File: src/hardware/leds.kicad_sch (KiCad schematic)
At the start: 74 parts

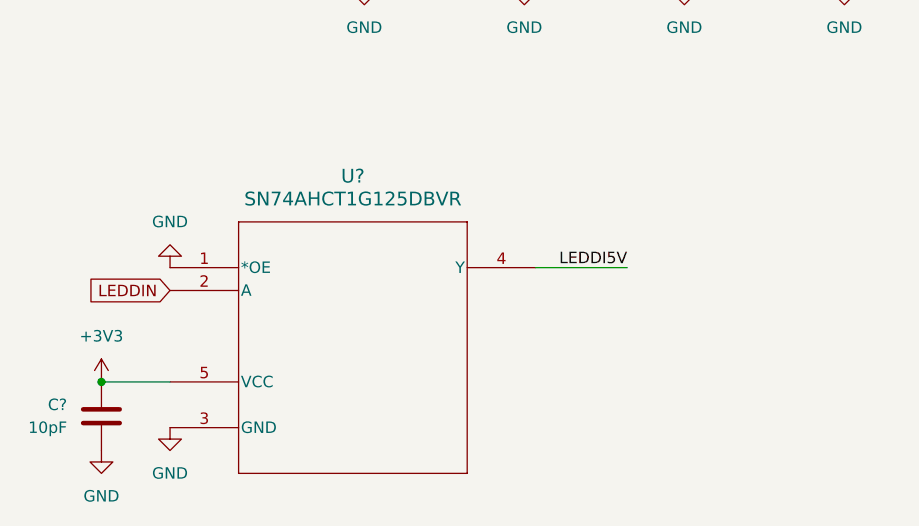
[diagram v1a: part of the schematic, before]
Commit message: Replaced schematics, 3d models and footprints. Added vibration motor.
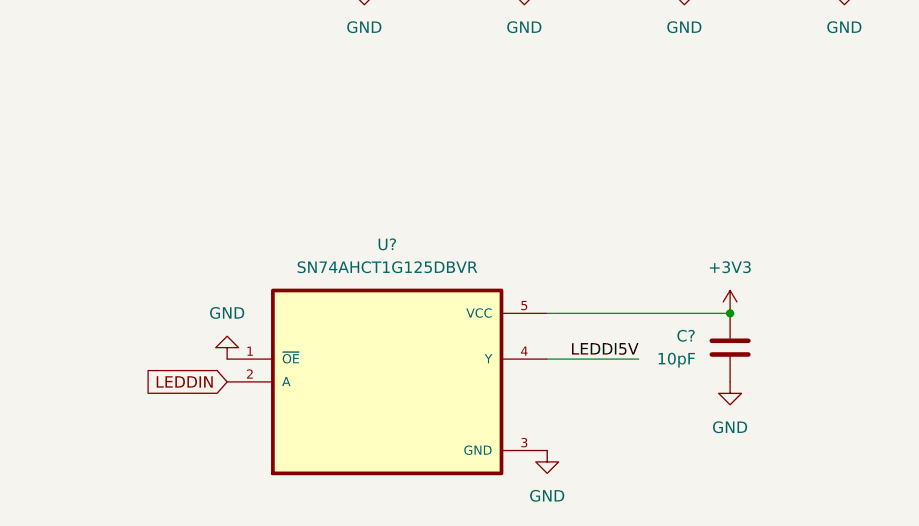
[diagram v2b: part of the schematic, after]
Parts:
- removed U?: SN74AHCT1G125DBVR, DBV5, symbol SN74AHCT1G125DBVR:SN74AHCT1G125DBVR
- added U?: SN74AHCT1G125DBVR, SN74AHCT1G125DBVR:SOT95P280X145-5N, symbol SN74AHCT1G125DBVR:SN74AHCT1G125DBVR
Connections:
- net +3V3: now also U?.5 (VCC)
- net GND: now also U?.1 (~{OE}), U?.3 (GND)
- net LEDDI5V: now also U?.4 (Y)
- net LEDDIN: now also U?.2 (A)
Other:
- moved on the sheet: C?

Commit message: Added LoRa
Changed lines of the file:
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@@
 		)
 		(property "Value" "+5V"
-			(at 48.26 31.75 0)
-			(effects
-				(font
-					(size 1.27 1.27)
-				)
+			(at 45.72 35.5599 0)
+			(effects
+				(font
+					(size 1.27 1.27)
+				)
+				(justify right)
 			)
 		)
@@
 		(fields_autoplaced yes)
 		(property "Reference" "C?"
-			(at 97.79 167.6399 0)
-			(effects
-				(font
-					(size 1.27 1.27)
-				)
-				(justify left)
+			(at 105.41 167.6399 0)
+			(effects
+				(font
+					(size 1.27 1.27)
+				)
+				(justify right)
 			)
 		)
 		(property "Value" "10pF"
-			(at 97.79 170.1799 0)
-			(effects
-				(font
-					(size 1.27 1.27)
-				)
-				(justify left)
+			(at 105.41 170.1799 0)
+			(effects
+				(font
+					(size 1.27 1.27)
+				)
+				(justify right)
 			)
 		)
@@
 		)
 		(property "Value" "GND"
-			(at 45.72 165.1 0)
-			(effects
-				(font
-					(size 1.27 1.27)
-				)
-			)
-		)
+			(at 43.18 168.9099 0)
+			(effects
+				(font
+					(size 1.27 1.27)
+				)
+				(justify right)
+			)
+		)

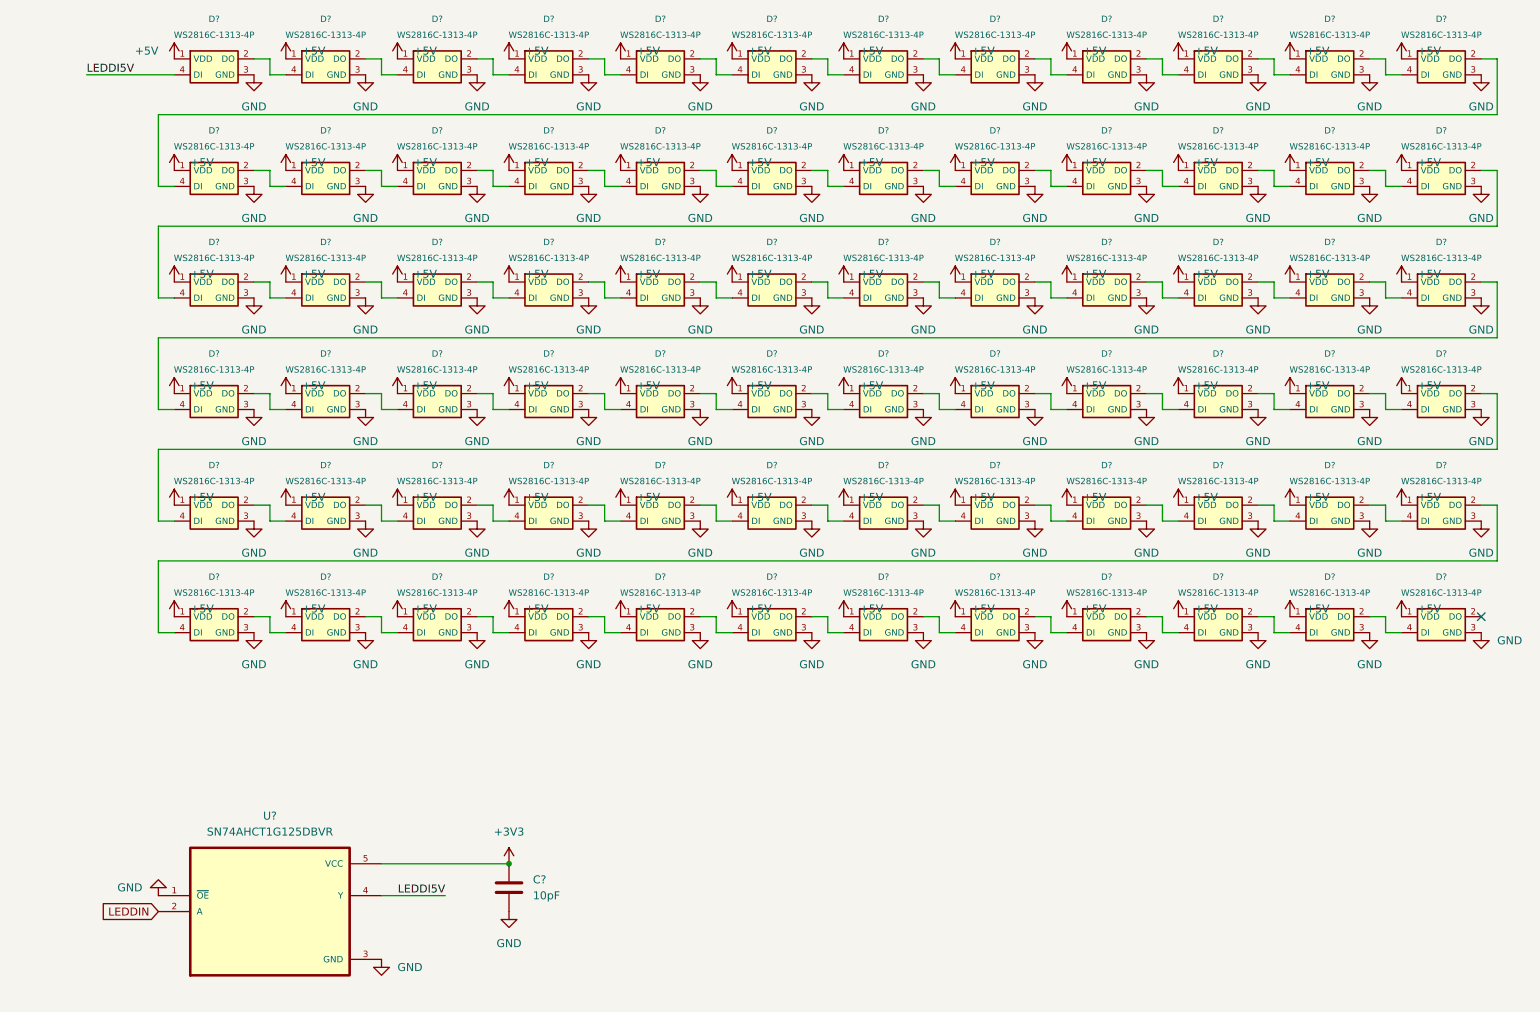
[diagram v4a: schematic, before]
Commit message: Changed 5V net to 4.5V net
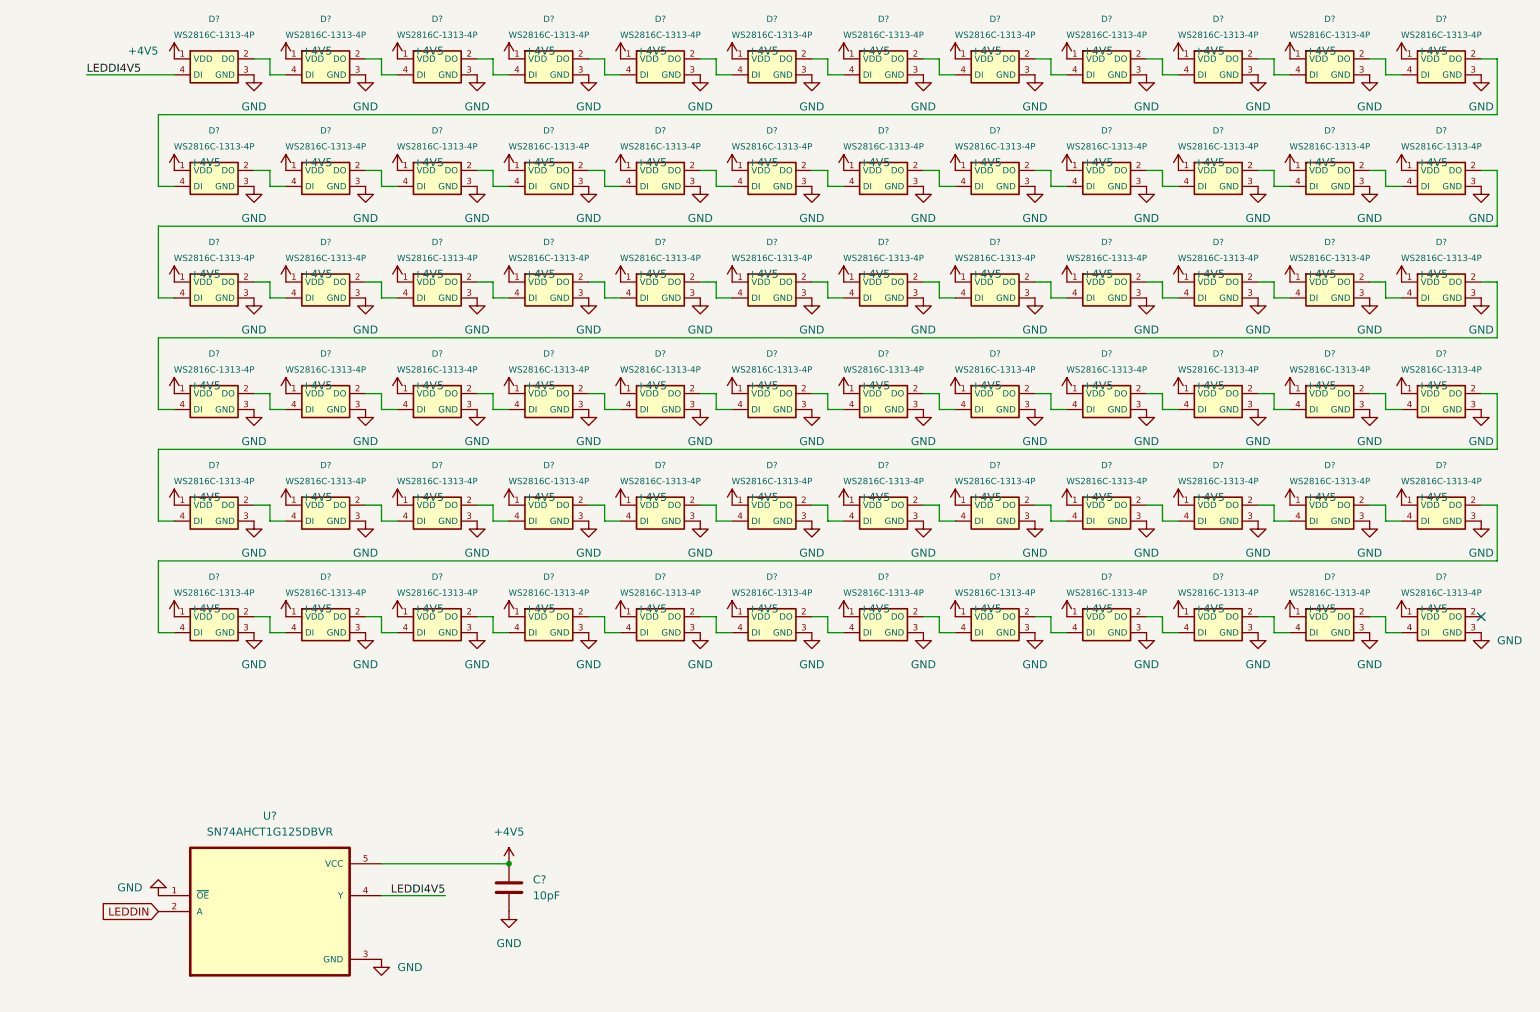
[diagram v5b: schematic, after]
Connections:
- net +5V is gone; now on net +4V5: D?.1 (VDD), D?.1 (VDD), D?.1 (VDD), D?.1 (VDD), D?.1 (VDD), D?.1 (VDD), D?.1 (VDD), D?.1 (VDD), D?.1 (VDD), D?.1 (VDD), D?.1 (VDD), D?.1 (VDD), D?.1 (VDD), D?.1 (VDD), D?.1 (VDD), D?.1 (VDD), D?.1 (VDD), D?.1 (VDD), D?.1 (VDD), D?.1 (VDD), D?.1 (VDD), D?.1 (VDD), D?.1 (VDD), D?.1 (VDD), D?.1 (VDD), D?.1 (VDD), D?.1 (VDD), D?.1 (VDD), D?.1 (VDD), D?.1 (VDD), D?.1 (VDD), D?.1 (VDD), D?.1 (VDD), D?.1 (VDD), D?.1 (VDD), D?.1 (VDD), D?.1 (VDD), D?.1 (VDD), D?.1 (VDD), D?.1 (VDD), D?.1 (VDD), D?.1 (VDD), D?.1 (VDD), D?.1 (VDD), D?.1 (VDD), D?.1 (VDD), D?.1 (VDD), D?.1 (VDD), D?.1 (VDD), D?.1 (VDD), D?.1 (VDD), D?.1 (VDD), D?.1 (VDD), D?.1 (VDD), D?.1 (VDD), D?.1 (VDD), D?.1 (VDD), D?.1 (VDD), D?.1 (VDD), D?.1 (VDD), D?.1 (VDD), D?.1 (VDD), D?.1 (VDD), D?.1 (VDD), D?.1 (VDD), D?.1 (VDD), D?.1 (VDD), D?.1 (VDD), D?.1 (VDD), D?.1 (VDD), D?.1 (VDD), D?.1 (VDD)
- net +3V3 renamed +4V5
- net LEDDI5V renamed LEDDI4V5

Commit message: Cleanup & Fixes; Added footprints; Removed Light sensors
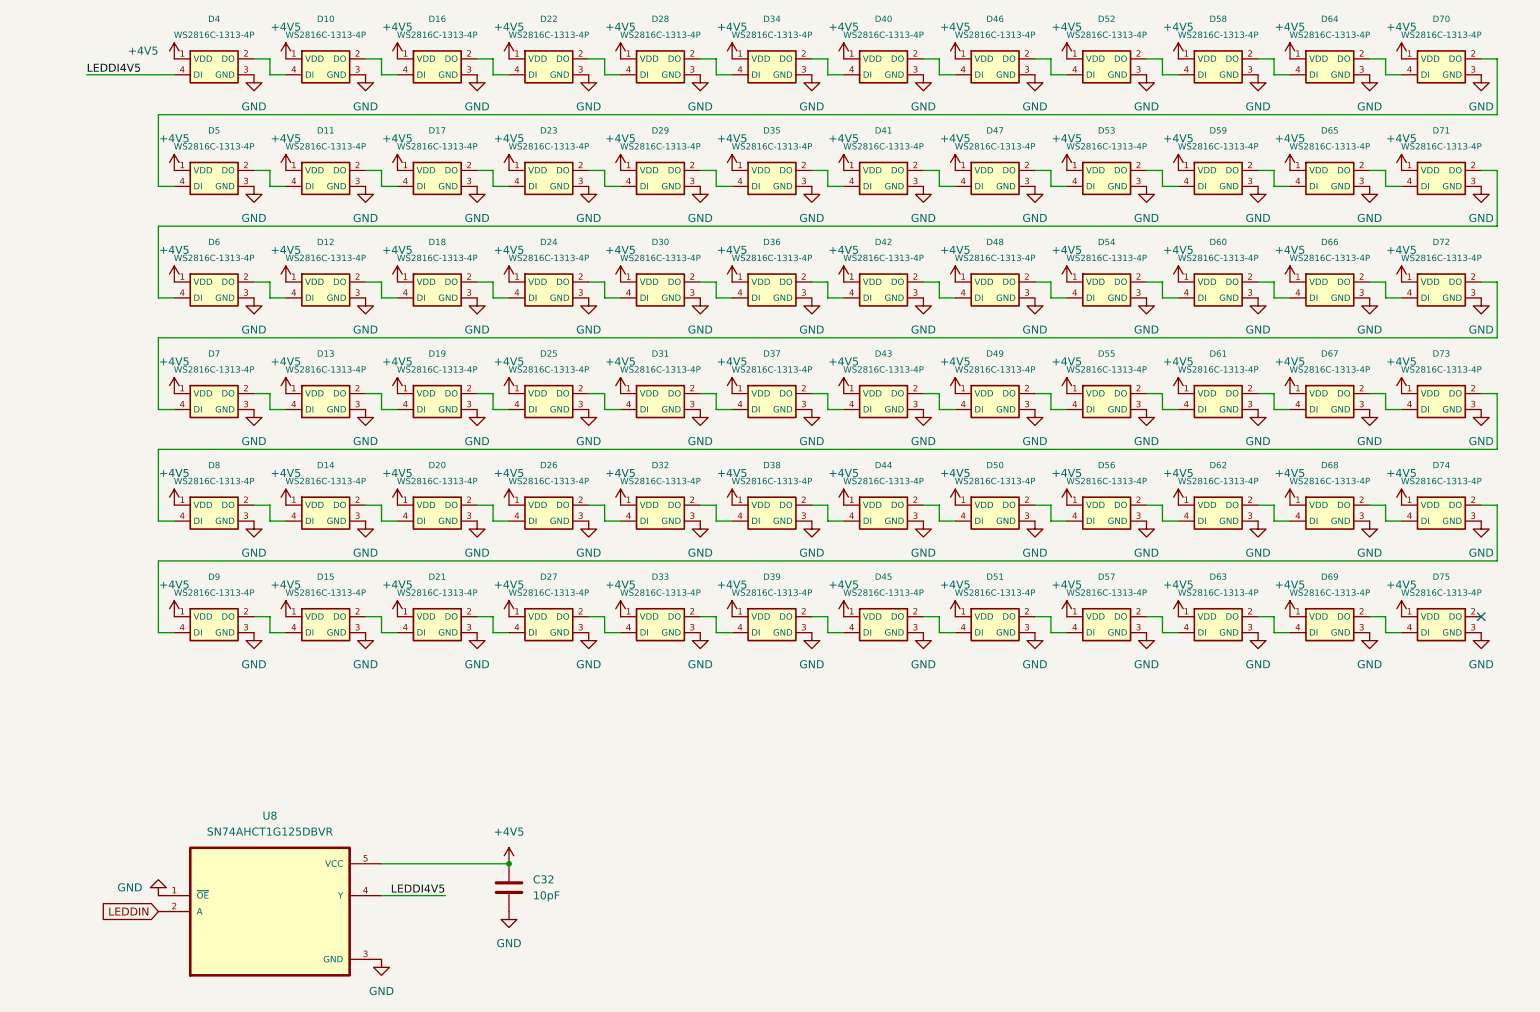
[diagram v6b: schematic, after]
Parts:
- C32: renamed from C?; footprint (none) -> Capacitor_SMD:C_0603_1608Metric
- D10, D11, D12, D13, D14, D15, D16, D17, D18, D19, D20, D21, D22, D23, D24, D25, D26, D27, D28, D29, D30, D31, D32, D33, D34, D35, D36, D37, D38, D39, D4, D40, D41, D42, D43, D44, D45, D46, D47, D48, D49, D5, D50, D51, D52, D53, D54, D55, D56, D57, D58, D59, D6, D60, D61, D62, D63, D64, D65, D66, D67, D68, D69, D7, D70, D71, D72, D73, D74, D75, D8, D9: renamed from D?; footprint WS2816C:WS2816C-1313-4P -> Project:WS2816C-1313-4P
- U8: renamed from U?; footprint SN74AHCT1G125DBVR:SOT95P280X145-5N -> Project:SOT95P280X145-5N

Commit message: Cleanup & Fixes; Changed GPIO; Added Camera; Added Microphone
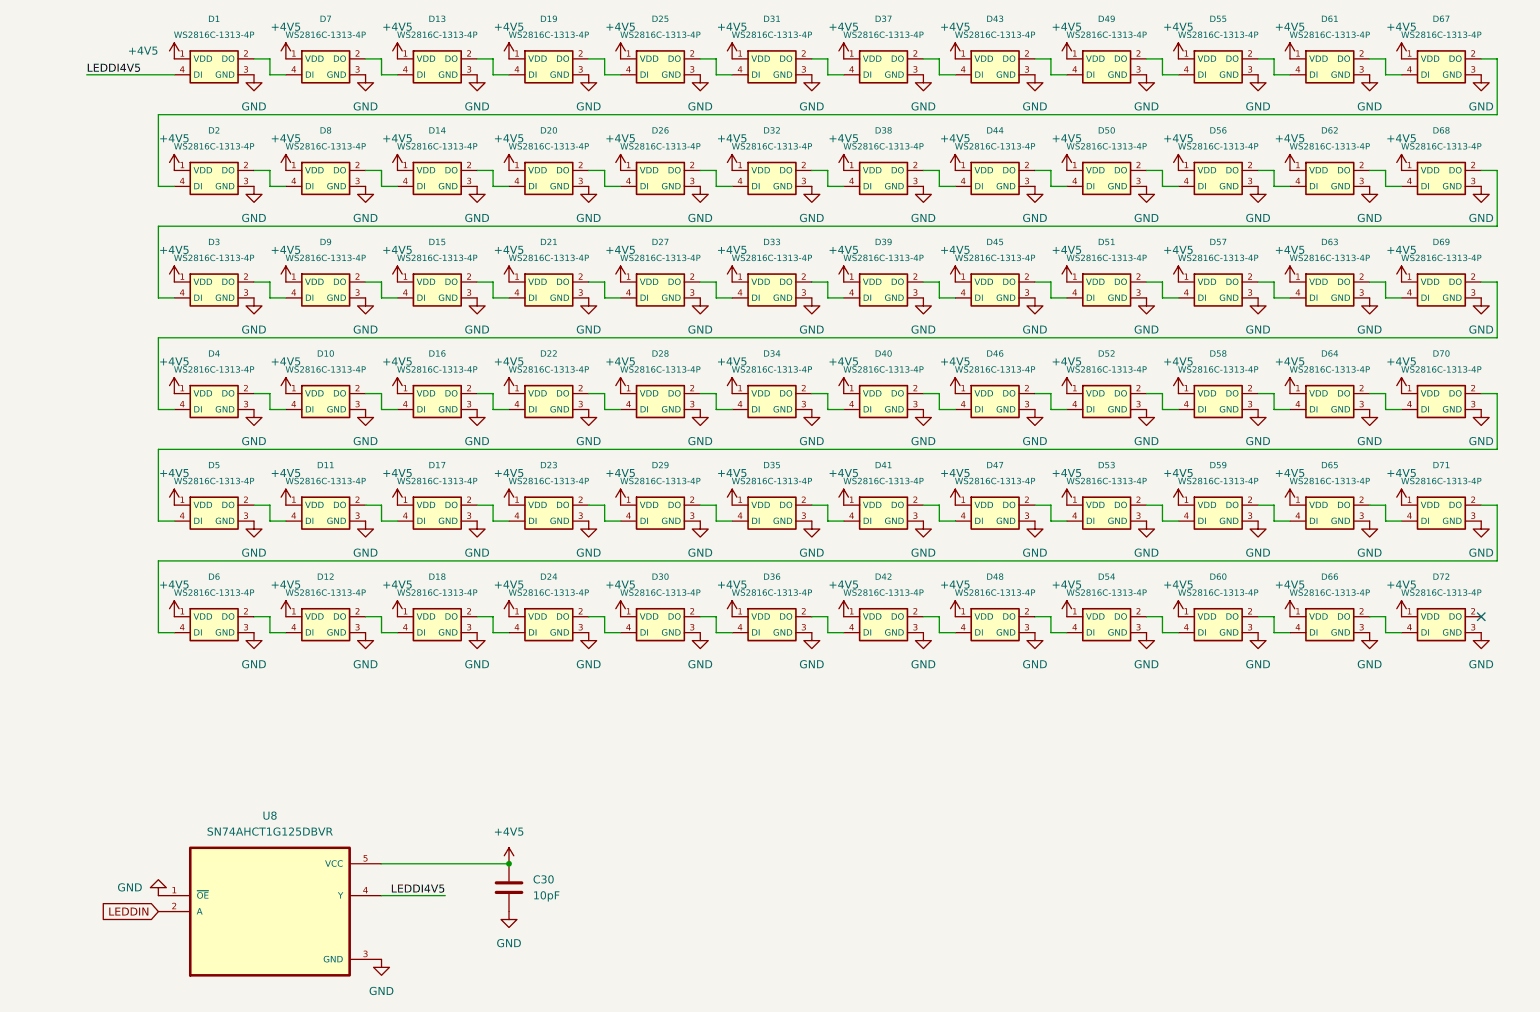
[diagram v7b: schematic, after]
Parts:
- renumbered C32 to C30, D4 to D1, D13 to D10, D14 to D11, D15 to D12, D16 to D13, D17 to D14, D18 to D15, D19 to D16, D20 to D17, D21 to D18, D22 to D19, D5 to D2, D23 to D20, D24 to D21, D25 to D22, D26 to D23, D27 to D24, D28 to D25, D29 to D26, D30 to D27, D31 to D28, D32 to D29, D6 to D3, D33 to D30, D34 to D31, D35 to D32, D36 to D33, D37 to D34, D38 to D35, D39 to D36, D40 to D37, D41 to D38, D42 to D39, D7 to D4, D43 to D40, D44 to D41, D45 to D42, D46 to D43, D47 to D44, D48 to D45, D49 to D46, D50 to D47, D51 to D48, D52 to D49, D8 to D5, D53 to D50, D54 to D51, D55 to D52, D56 to D53, D57 to D54, D58 to D55, D59 to D56, D60 to D57, D61 to D58, D62 to D59, D9 to D6, D63 to D60, D64 to D61, D65 to D62, D66 to D63, D67 to D64, D68 to D65, D69 to D66, D70 to D67, D71 to D68, D72 to D69, D10 to D7, D73 to D70, D74 to D71, D75 to D72, D11 to D8, D12 to D9

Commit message: Add Light Sensor and Proximity & Gesture Sensor; Changed GPIO
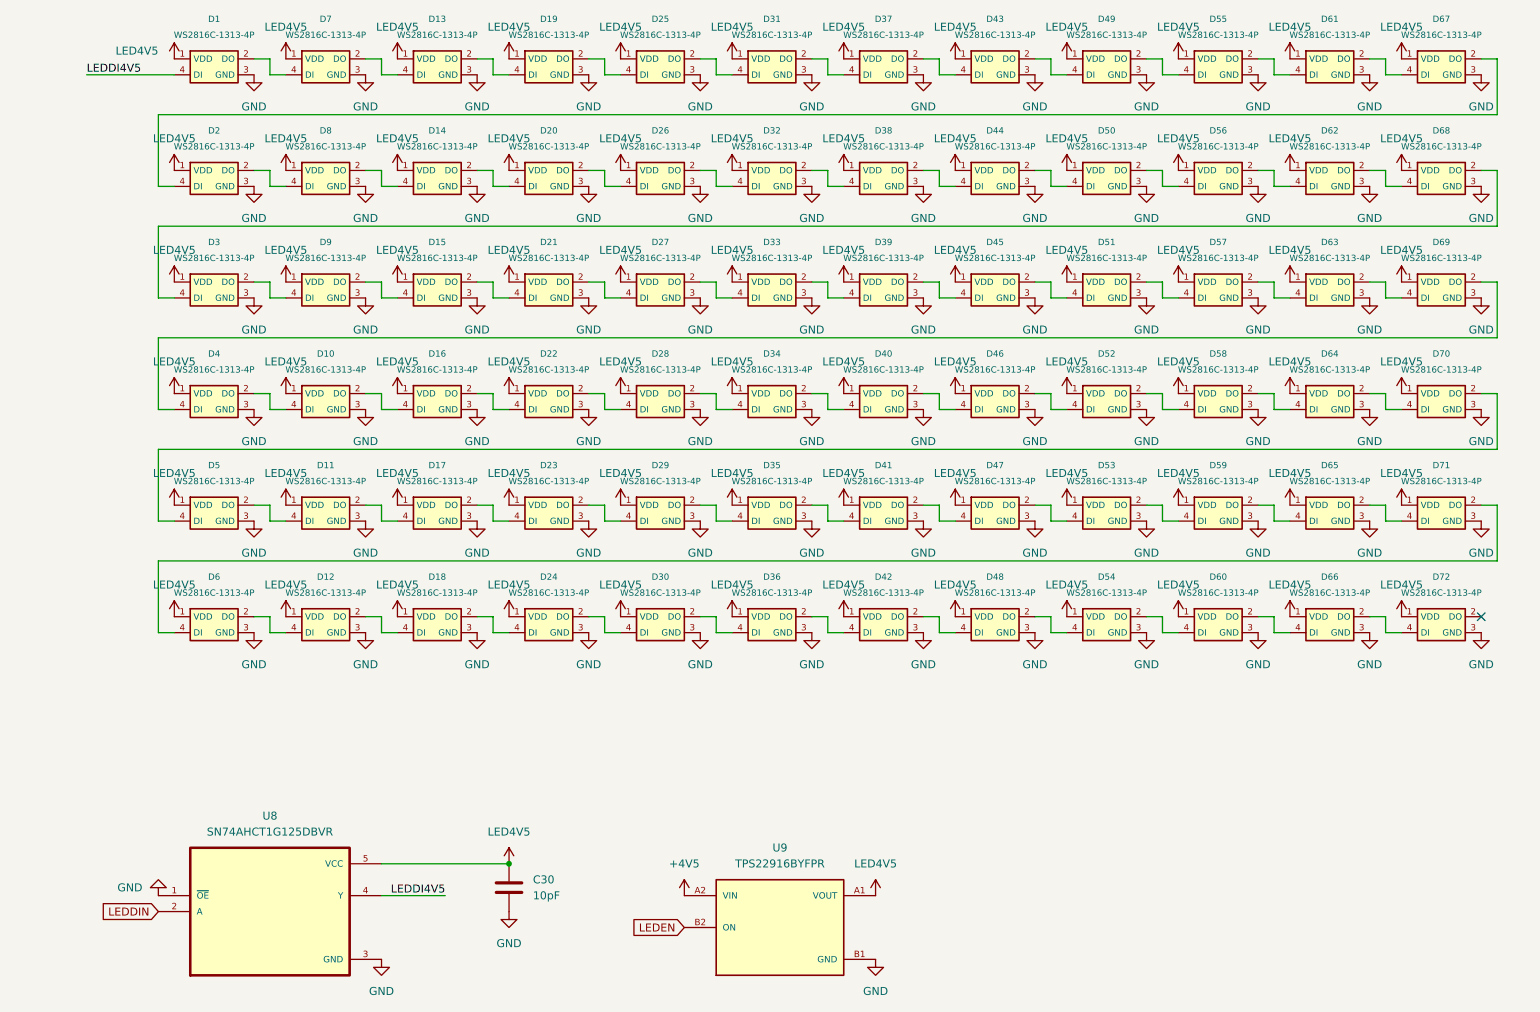
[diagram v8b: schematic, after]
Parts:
- added U9: TPS22916BYFPR, Project:IC_TPS22916BYFPR, symbol TPS22916BYFPR:TPS22916BYFPR
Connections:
- net +4V5: now also U9.A2 (VIN); no longer C30.1, D1.1 (VDD), D10.1 (VDD), D11.1 (VDD), D12.1 (VDD), D13.1 (VDD), D14.1 (VDD), D15.1 (VDD), D16.1 (VDD), D17.1 (VDD), D18.1 (VDD), D19.1 (VDD), D2.1 (VDD), D20.1 (VDD), D21.1 (VDD), D22.1 (VDD), D23.1 (VDD), D24.1 (VDD), D25.1 (VDD), D26.1 (VDD), D27.1 (VDD), D28.1 (VDD), D29.1 (VDD), D3.1 (VDD), D30.1 (VDD), D31.1 (VDD), D32.1 (VDD), D33.1 (VDD), D34.1 (VDD), D35.1 (VDD), D36.1 (VDD), D37.1 (VDD), D38.1 (VDD), D39.1 (VDD), D4.1 (VDD), D40.1 (VDD), D41.1 (VDD), D42.1 (VDD), D43.1 (VDD), D44.1 (VDD), D45.1 (VDD), D46.1 (VDD), D47.1 (VDD), D48.1 (VDD), D49.1 (VDD), D5.1 (VDD), D50.1 (VDD), D51.1 (VDD), D52.1 (VDD), D53.1 (VDD), D54.1 (VDD), D55.1 (VDD), D56.1 (VDD), D57.1 (VDD), D58.1 (VDD), D59.1 (VDD), D6.1 (VDD), D60.1 (VDD), D61.1 (VDD), D62.1 (VDD), D63.1 (VDD), D64.1 (VDD), D65.1 (VDD), D66.1 (VDD), D67.1 (VDD), D68.1 (VDD), D69.1 (VDD), D7.1 (VDD), D70.1 (VDD), D71.1 (VDD), D72.1 (VDD), D8.1 (VDD), D9.1 (VDD), U8.5 (VCC)
- net GND: now also U9.B1 (GND)
- new net LED4V5: C30.1, D1.1 (VDD), D10.1 (VDD), D11.1 (VDD), D12.1 (VDD), D13.1 (VDD), D14.1 (VDD), D15.1 (VDD), D16.1 (VDD), D17.1 (VDD), D18.1 (VDD), D19.1 (VDD), D2.1 (VDD), D20.1 (VDD), D21.1 (VDD), D22.1 (VDD), D23.1 (VDD), D24.1 (VDD), D25.1 (VDD), D26.1 (VDD), D27.1 (VDD), D28.1 (VDD), D29.1 (VDD), D3.1 (VDD), D30.1 (VDD), D31.1 (VDD), D32.1 (VDD), D33.1 (VDD), D34.1 (VDD), D35.1 (VDD), D36.1 (VDD), D37.1 (VDD), D38.1 (VDD), D39.1 (VDD), D4.1 (VDD), D40.1 (VDD), D41.1 (VDD), D42.1 (VDD), D43.1 (VDD), D44.1 (VDD), D45.1 (VDD), D46.1 (VDD), D47.1 (VDD), D48.1 (VDD), D49.1 (VDD), D5.1 (VDD), D50.1 (VDD), D51.1 (VDD), D52.1 (VDD), D53.1 (VDD), D54.1 (VDD), D55.1 (VDD), D56.1 (VDD), D57.1 (VDD), D58.1 (VDD), D59.1 (VDD), D6.1 (VDD), D60.1 (VDD), D61.1 (VDD), D62.1 (VDD), D63.1 (VDD), D64.1 (VDD), D65.1 (VDD), D66.1 (VDD), D67.1 (VDD), D68.1 (VDD), D69.1 (VDD), D7.1 (VDD), D70.1 (VDD), D71.1 (VDD), D72.1 (VDD), D8.1 (VDD), D9.1 (VDD), U8.5 (VCC), U9.A1 (VOUT)
- new net LEDEN: U9.B2 (ON)
